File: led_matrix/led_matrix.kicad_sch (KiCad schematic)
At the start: 13 parts, among them J101 Conn_02x08_Odd_Even, J102 Conn_01x02, U101 74HC245, U102 74HC245, U103 74154, U104 74154, U105 Inverter_Schmitt_Dual, U106 FDS4935A

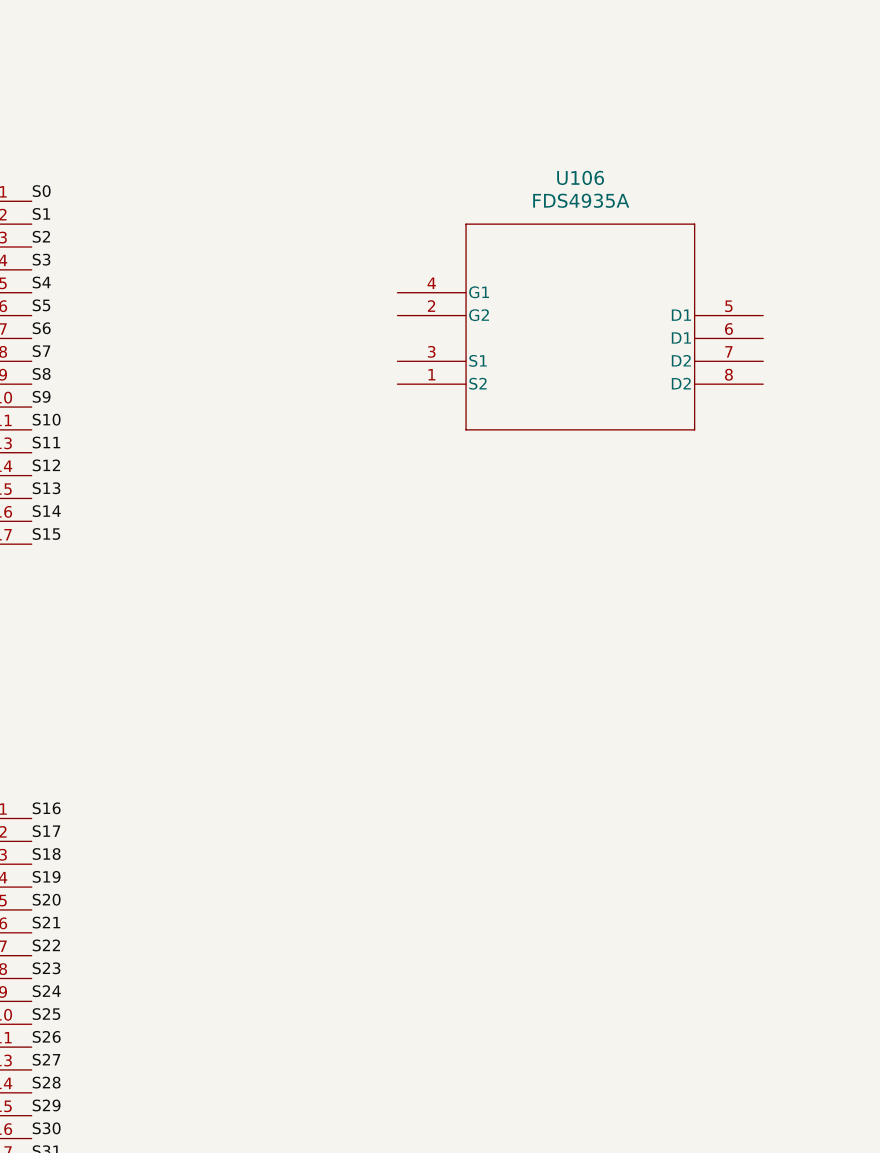
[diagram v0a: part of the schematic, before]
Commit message: created mosfet array to drive LEDs. added gitignore
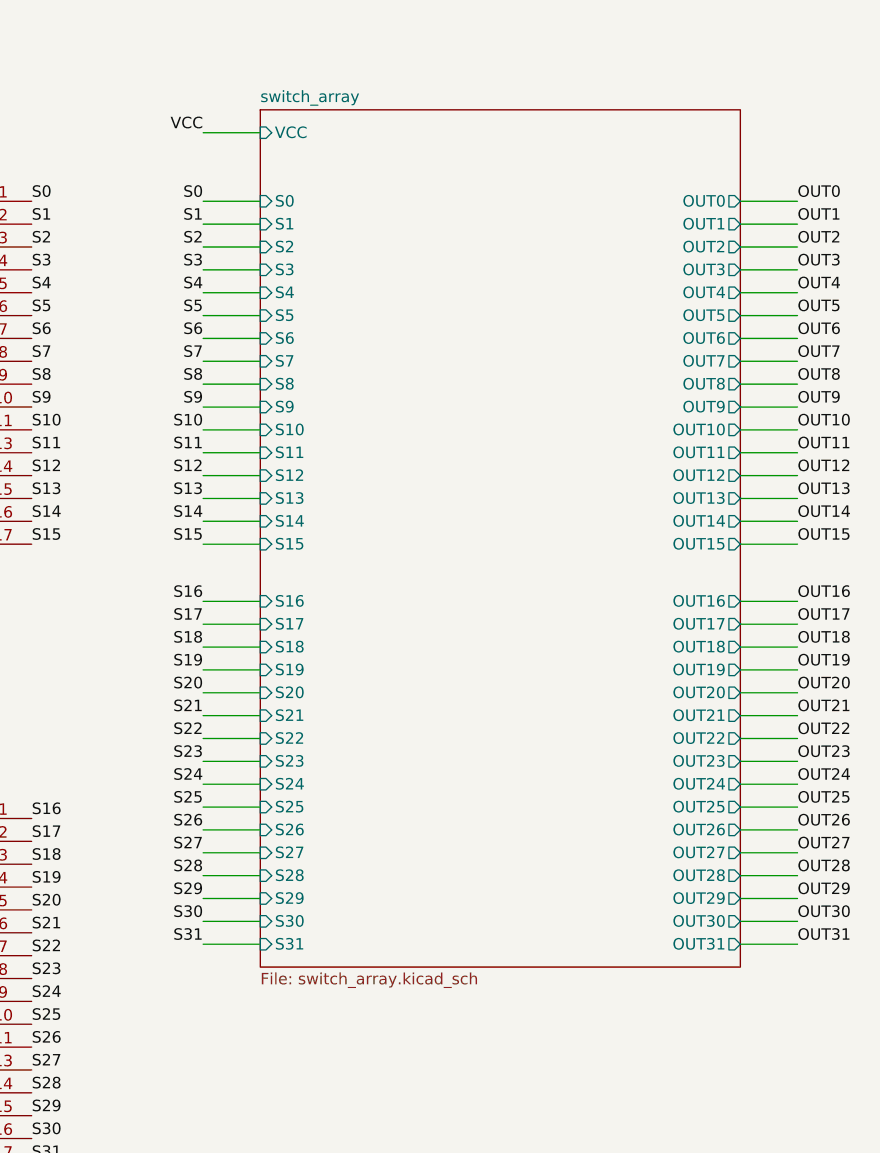
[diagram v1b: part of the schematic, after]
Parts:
- removed U106: FDS4935A, SO-8_ONS, symbol FDS4935:FDS4935A
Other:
- added sheet switch_array (switch_array.kicad_sch)

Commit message: abstract input sanitation
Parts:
- removed C101, C102, C103, C104, C105: 0.1uF, symbol Device:C
- removed U101, U102: 74HC245, symbol 74xx:74HC245
- removed U103, U104: 74154, symbol 74xx_IEEE:74154
- removed U105: Inverter_Schmitt_Dual, symbol 74xGxx:Inverter_Schmitt_Dual
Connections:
- no-connect marks 4 -> 0
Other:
- added sheet input_sanitation (input_sanitation.kicad_sch)
- moved on the sheet: J101, J102
